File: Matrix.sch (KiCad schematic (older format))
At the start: 227 parts

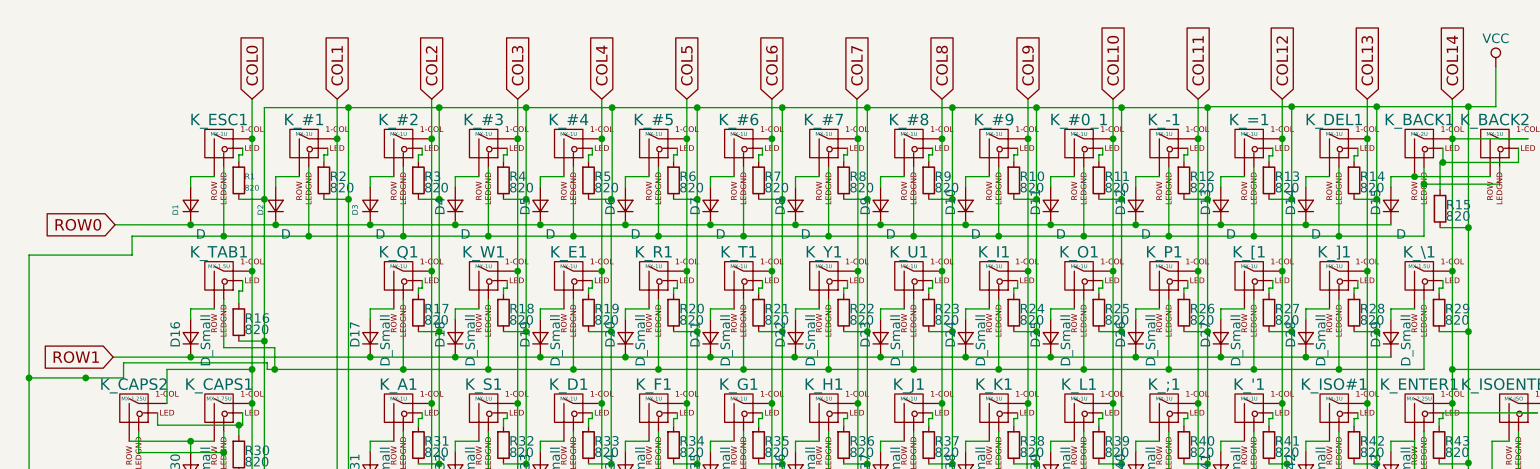
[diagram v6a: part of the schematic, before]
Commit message: Update: Rename some diodes to be consistent
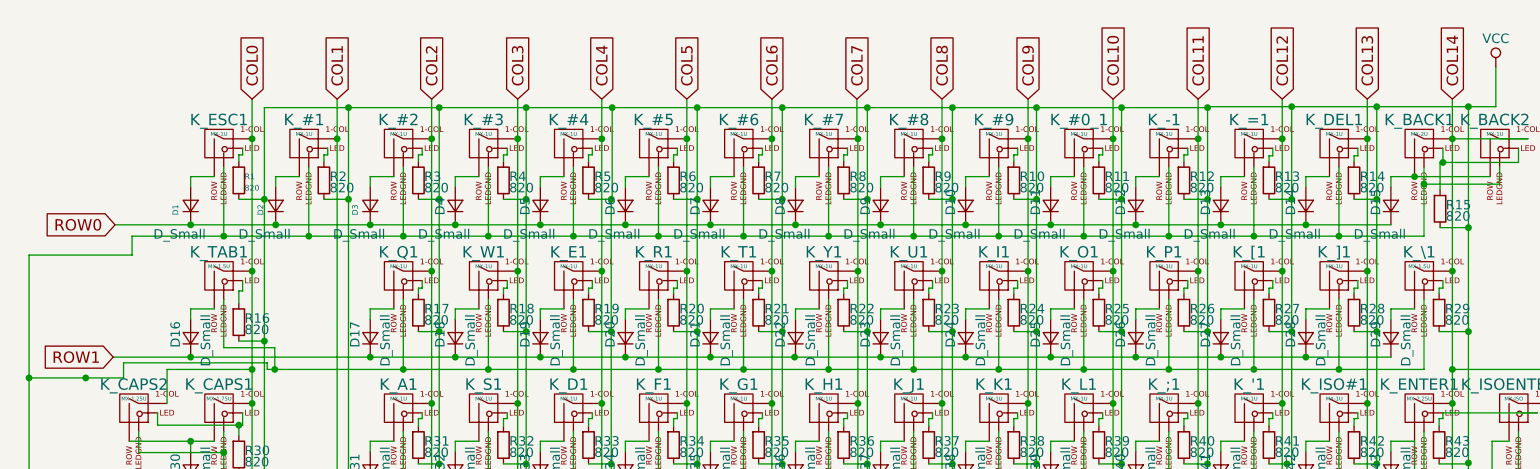
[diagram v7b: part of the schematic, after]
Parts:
- D1, D10, D11, D12, D13, D14, D15, D2, D3, D4, D5, D6, D7, D8, D9: value D -> D_Small
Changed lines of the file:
@@
 P 1400 1430
 F 0 "D1" H 1350 1510 30  0000 L CNN
-F 1 "D" V 1250 1350 50  0000 L CNN
+F 1 "D_Small" V 1250 1350 50  0000 L CNN
 F 2 "Diodes_SMD:D_SOD-123" V 1400 1430 50  0001 C CNN
 F 3 "" V 1400 1430 50  0001 C CNN
@@
 P 1850 1430
 F 0 "D2" H 1800 1510 30  0000 L CNN
-F 1 "D" V 1700 1350 50  0000 L CNN
+F 1 "D_Small" V 1700 1350 50  0000 L CNN
 F 2 "Diodes_SMD:D_SOD-123" V 1850 1430 50  0001 C CNN
 F 3 "" V 1850 1430 50  0001 C CNN
@@
 P 2350 1430
 F 0 "D3" H 2300 1510 30  0000 L CNN
-F 1 "D" V 2200 1350 50  0000 L CNN
+F 1 "D_Small" V 2200 1350 50  0000 L CNN
 F 2 "Diodes_SMD:D_SOD-123" V 2350 1430 50  0001 C CNN
 F 3 "" V 2350 1430 50  0001 C CNN
@@
 P 2800 1430
 F 0 "D4" H 2750 1510 50  0000 L CNN
-F 1 "D" V 2650 1350 50  0000 L CNN
+F 1 "D_Small" V 2650 1350 50  0000 L CNN
 F 2 "Diodes_SMD:D_SOD-123" V 2800 1430 50  0001 C CNN
 F 3 "" V 2800 1430 50  0001 C CNN
@@
 P 3250 1430
 F 0 "D5" H 3200 1510 50  0000 L CNN
-F 1 "D" V 3100 1350 50  0000 L CNN
+F 1 "D_Small" V 3100 1350 50  0000 L CNN
 F 2 "Diodes_SMD:D_SOD-123" V 3250 1430 50  0001 C CNN
 F 3 "" V 3250 1430 50  0001 C CNN
@@
 P 3700 1430
 F 0 "D6" H 3650 1510 50  0000 L CNN
-F 1 "D" V 3550 1350 50  0000 L CNN
+F 1 "D_Small" V 3550 1350 50  0000 L CNN
 F 2 "Diodes_SMD:D_SOD-123" V 3700 1430 50  0001 C CNN
 F 3 "" V 3700 1430 50  0001 C CNN
@@
 P 4150 1430
 F 0 "D7" H 4100 1510 50  0000 L CNN
-F 1 "D" V 4000 1350 50  0000 L CNN
+F 1 "D_Small" V 4000 1350 50  0000 L CNN
 F 2 "Diodes_SMD:D_SOD-123" V 4150 1430 50  0001 C CNN
 F 3 "" V 4150 1430 50  0001 C CNN
@@
 P 4600 1430
 F 0 "D8" H 4550 1510 50  0000 L CNN
-F 1 "D" V 4450 1350 50  0000 L CNN
+F 1 "D_Small" V 4450 1350 50  0000 L CNN
 F 2 "Diodes_SMD:D_SOD-123" V 4600 1430 50  0001 C CNN
 F 3 "" V 4600 1430 50  0001 C CNN
@@
 P 5050 1430
 F 0 "D9" H 5000 1510 50  0000 L CNN
-F 1 "D" V 4900 1350 50  0000 L CNN
+F 1 "D_Small" V 4900 1350 50  0000 L CNN
 F 2 "Diodes_SMD:D_SOD-123" V 5050 1430 50  0001 C CNN
 F 3 "" V 5050 1430 50  0001 C CNN
@@
 P 5500 1430
 F 0 "D10" H 5450 1510 50  0000 L CNN
-F 1 "D" V 5350 1350 50  0000 L CNN
+F 1 "D_Small" V 5350 1350 50  0000 L CNN
 F 2 "Diodes_SMD:D_SOD-123" V 5500 1430 50  0001 C CNN
 F 3 "" V 5500 1430 50  0001 C CNN
@@
 P 5950 1430
 F 0 "D11" H 5900 1510 50  0000 L CNN
-F 1 "D" V 5800 1350 50  0000 L CNN
+F 1 "D_Small" V 5800 1350 50  0000 L CNN
 F 2 "Diodes_SMD:D_SOD-123" V 5950 1430 50  0001 C CNN
 F 3 "" V 5950 1430 50  0001 C CNN
@@
 P 6400 1430
 F 0 "D12" H 6350 1510 50  0000 L CNN
-F 1 "D" V 6250 1350 50  0000 L CNN
+F 1 "D_Small" V 6250 1350 50  0000 L CNN
 F 2 "Diodes_SMD:D_SOD-123" V 6400 1430 50  0001 C CNN
 F 3 "" V 6400 1430 50  0001 C CNN
@@
 P 6850 1430
 F 0 "D13" H 6800 1510 50  0000 L CNN
-F 1 "D" V 6700 1350 50  0000 L CNN
+F 1 "D_Small" V 6700 1350 50  0000 L CNN
 F 2 "Diodes_SMD:D_SOD-123" V 6850 1430 50  0001 C CNN
 F 3 "" V 6850 1430 50  0001 C CNN
@@
 P 7300 1430
 F 0 "D14" H 7250 1510 50  0000 L CNN
-F 1 "D" V 7150 1350 50  0000 L CNN
+F 1 "D_Small" V 7150 1350 50  0000 L CNN
 F 2 "Diodes_SMD:D_SOD-123" V 7300 1430 50  0001 C CNN
 F 3 "" V 7300 1430 50  0001 C CNN
@@
 P 7750 1430
 F 0 "D15" H 7700 1510 50  0000 L CNN
-F 1 "D" V 7600 1350 50  0000 L CNN
+F 1 "D_Small" V 7600 1350 50  0000 L CNN
 F 2 "Diodes_SMD:D_SOD-123" V 7750 1430 50  0001 C CNN
 F 3 "" V 7750 1430 50  0001 C CNN

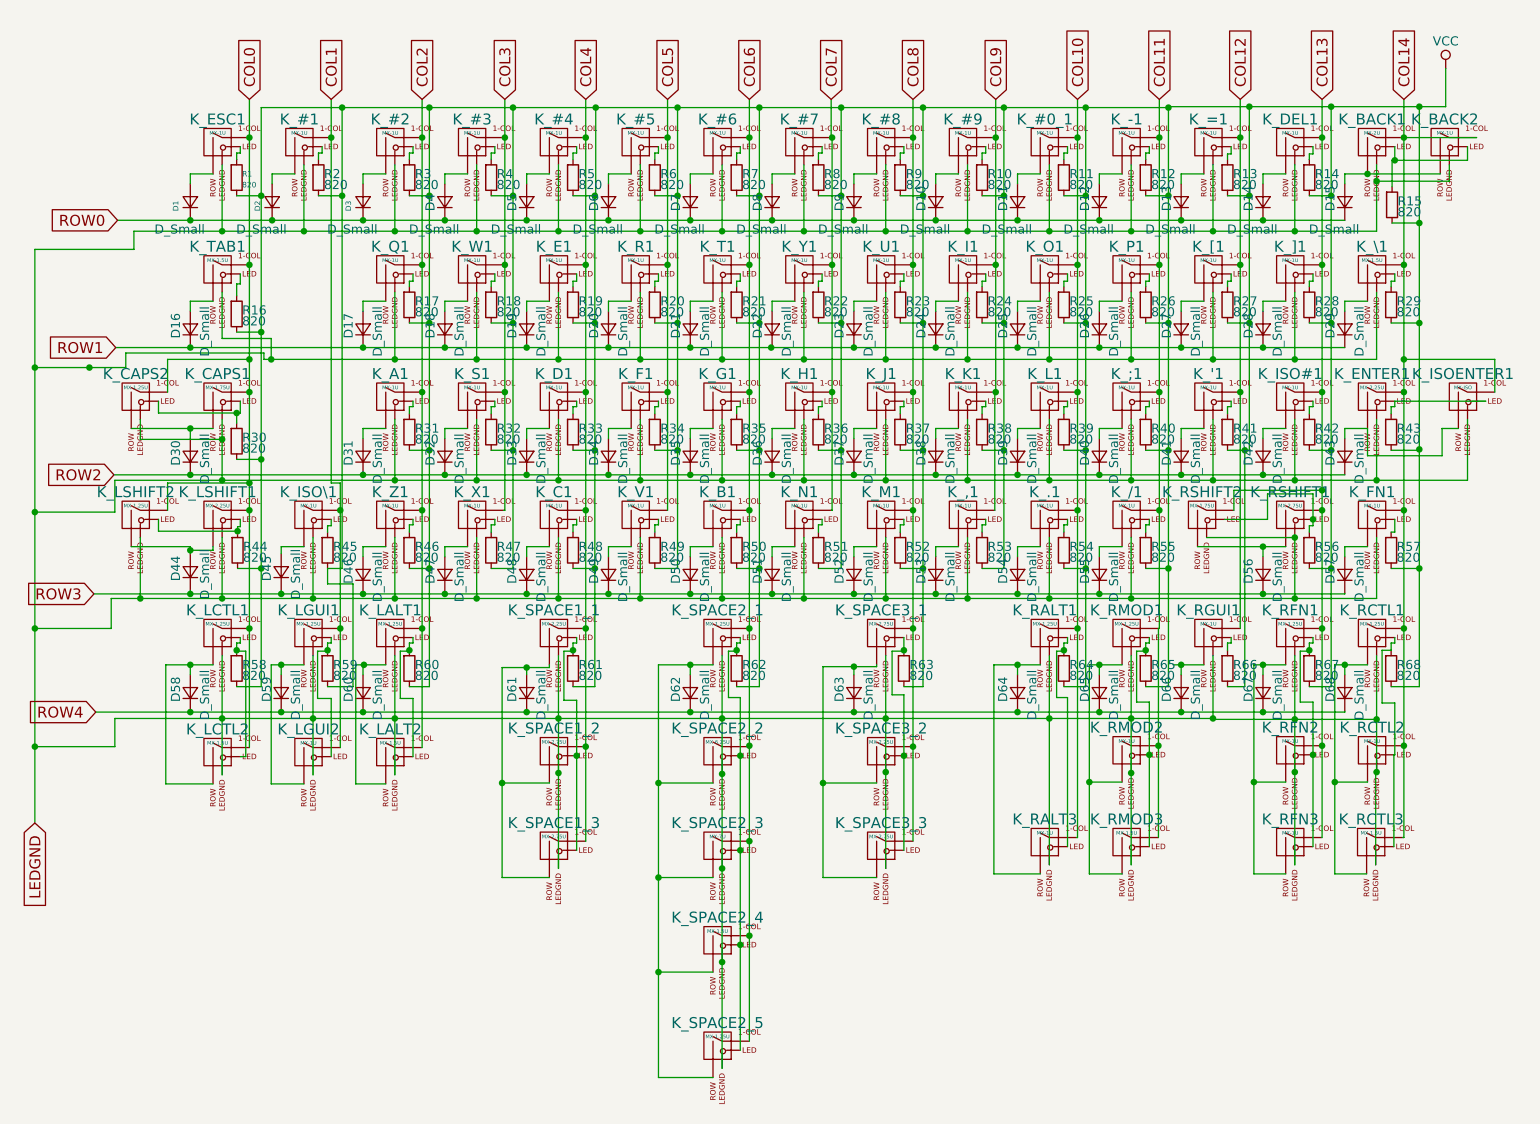
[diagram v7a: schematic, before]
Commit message: Update: Switch resistors to 560 Ohm, and separate footprints
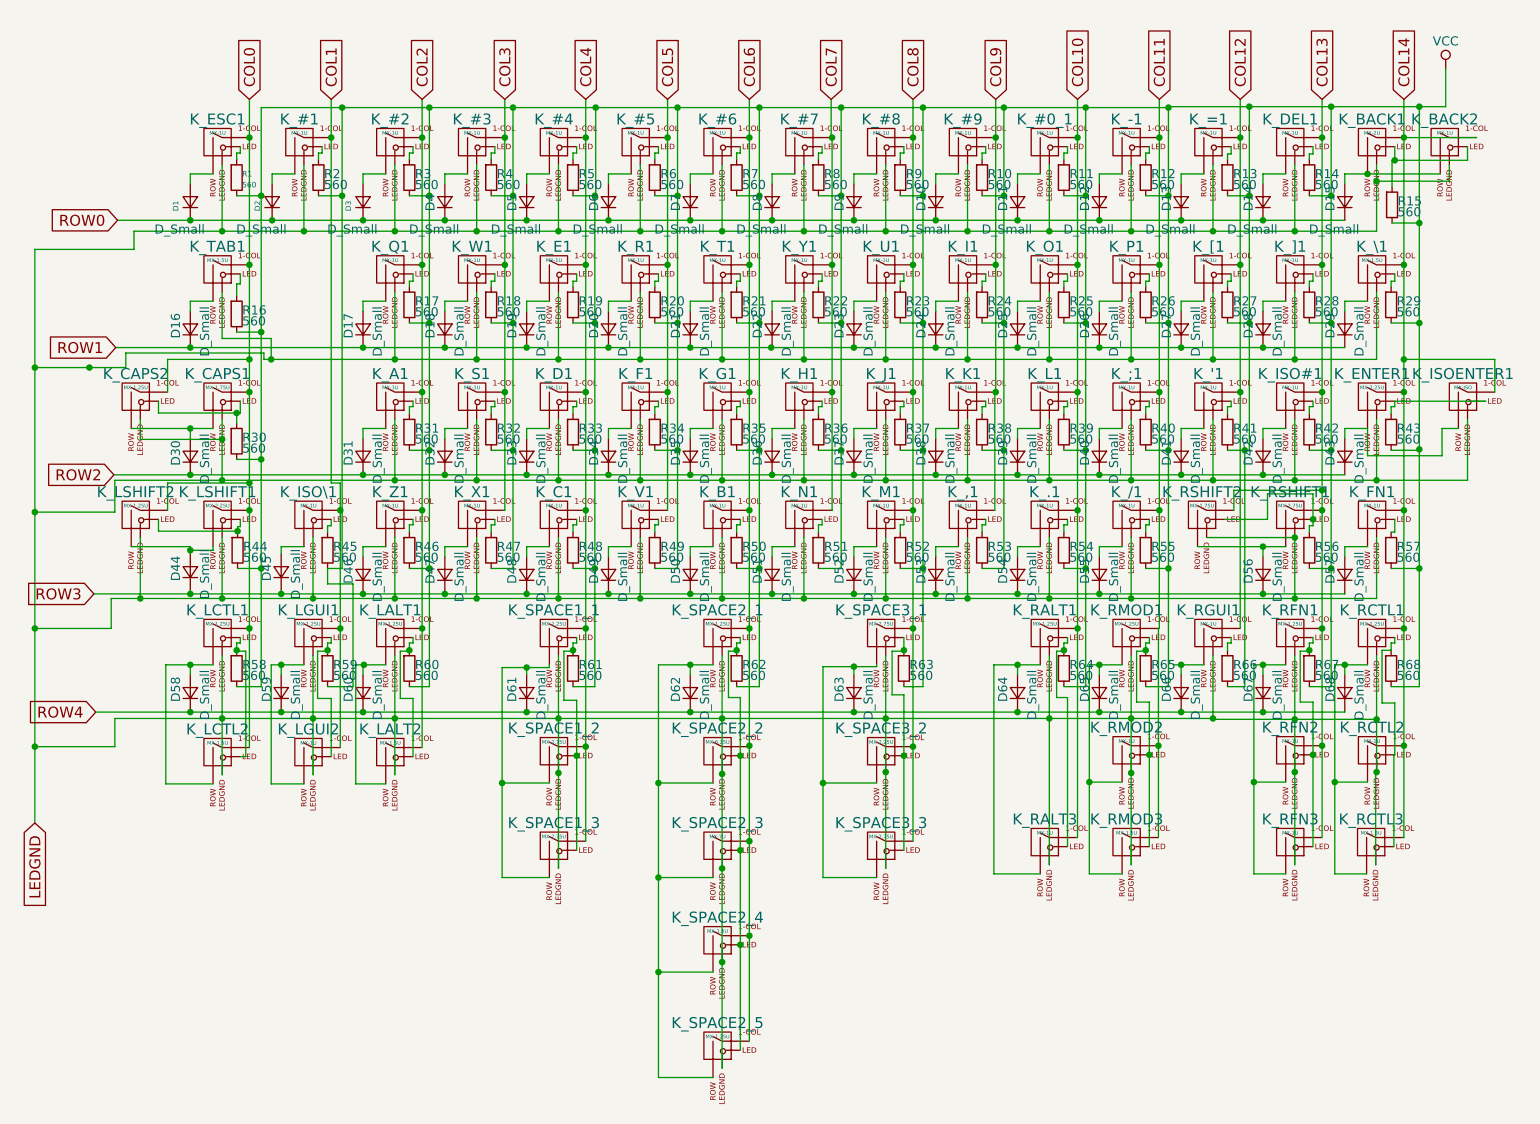
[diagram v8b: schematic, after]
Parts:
- R1, R10, R11, R12, R13, R14, R15, R16, R17, R18, R19, R2, R20, R21, R22, R23, R24, R25, R26, R27, R28, R29, R3, R30, R31, R32, R33, R34, R35, R36, R37, R38, R39, R4, R40, R41, R42, R43, R44, R45, R46, R47, R48, R49, R5, R50, R51, R52, R53, R54, R55, R56, R57, R58, R59, R6, R60, R61, R62, R63, R64, R65, R66, R67, R68, R7, R8, R9: value 820 -> 560
